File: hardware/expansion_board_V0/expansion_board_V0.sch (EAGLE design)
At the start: 109 parts, among them IC6 DRV8402, IC7 DRV8402, IC8 DRV8402, X10 M1-2, X11 M3-4, X14 M1-2, X15 M3-4, X18 M1-2, X19 M3-4

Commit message: Add some I/Os connectors
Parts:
- removed C48, C49, C50, C51: 100n, rcl:C-EUC0805
- removed C52, C53, C54, C55: 100n, rcl:C-EUC0603
- removed C56: 100n, rcl:C-EUC0603K
- removed IC8: DRV8402, etienne:DRV8402
- removed JP2, JP3, JP4: (no value), pinhead-2:PINHD-1X08_2.54
- removed X16, X17: (no value), con-phoenix-254:MPT2
- removed X18: M1-2, con-wago-500:W237-102
- removed X19: M3-4, con-wago-500:W237-102
- removed X2: (no value), con-phoenix-254:MPT4
- added C1, C2, C3, C6: 100n, rcl:C-EUC0805
- added C11, C7, C8, C9: 100n, rcl:C-EUC0603
- added C17: 100n, rcl:C-EUC0603K
- added IC1: DRV8402, etienne:DRV8402
- added J1, J10, J11, J12, J13, J14, J15, J16, J2, J24, J25, J26, J3, J4, J5, J6, J7, J8, J9: (no value), SparkFun-Connectors:M03LONGPADS
- added J17, J20, J21, J22: (no value), SparkFun-Connectors:M08LONGPADS
- added J18, J19: (no value), SparkFun-Connectors:M04JST
- added J23: (no value), SparkFun-Connectors:M04POLAR
- added J27, J28, J29, J30, J31, J32: (no value), SparkFun-Connectors:M03JST-PTH-VERT
- added R10, R12, R22, R23, R24, R25, R26, R27, R28, R29, R30, R31, R32, R33, R34, R35, R36, R37, R38, R39, R40, R41, R42, R43, R44, R45, R46, R47, R48, R49, R50, R9: (no value), resistor:R-EU_R0603
- added R51, R52: 33R, resistor:R-EU_R0603
- added X1, X3: (no value), con-phoenix-254:MPT2
- added X4: M1-2, con-wago-500:W237-102
- added X5: M3-4, con-wago-500:W237-102
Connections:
- removed net N$100: IC8.M2, R18.1
- removed net N$101: IC8.M3, R17.1
- removed net N$102: C50.2, IC8.BST_A
- removed net N$103: C49.2, IC8.BST_B
- removed net N$104: C48.1, IC8.BST_C
- removed net N$105: C51.1, IC8.BST_D
- removed net N$106: C56.2, IC8.AGND, R17.2, R18.2, R19.2, R20.2, R21.1
- removed net N$114: C56.1, IC8.VREG
- removed net N$115: IC8.OC_ADJ, R21.2
- removed net N$116: IC8.OTW, JP4.8
- removed net N$117: IC8.FAULT, JP4.7
- removed net N$118: IC8.PWM_A, JP4.6
- removed net N$119: IC8.RESET_AB, JP4.5
- removed net N$120: IC8.PWM_B, JP4.4
- removed net N$121: IC8.PWM_C, JP4.3
- removed net N$122: IC8.RESET_CD, JP4.2
- removed net N$123: IC8.PWM_D, JP4.1
- removed net N$5: X2-2.1
- removed net N$99: IC8.M1, R19.1
- new net /SS1: J18.1
- new net /SS2: J19.1
- new net AN_1: R35.2, R36.2
- new net AN_2: R37.2, R38.2
- new net AN_3: R39.2, R40.2
- new net AN_4: R41.2, R42.2
- new net AN_5: R43.2, R44.2
- new net AN_6: R45.2, R46.2
- new net AN_7: R47.2, R48.2
- new net AN_8: R49.2, R50.2
- new net D1: J20.8
- new net D2: J20.7
- new net D3: J20.6
- new net D4: J20.5
- new net D5: J20.4
- new net D6: J20.3
- new net D7: J20.2
- new net D8: J20.1
- new net IND_1: J27.1
- new net IND_2: J28.1
- new net IND_3: J29.1
- new net IND_4: J30.1
- new net IND_5: J31.1
- new net IND_6: J32.1
- new net MISO1: J18.4
- new net MISO2: J19.4
- new net MOSI1: J18.3, R51.1, R51.2
- new net MOSI2: J19.3, R52.1, R52.2
- new net N$10: J12.3, R41.1
- new net N$11: J2.3, R12.1
- new net N$12: J13.3, R43.1
- new net N$13: J3.3, R23.1
- new net N$14: J14.3, R45.1
- new net N$15: J4.3, R25.1
- new net N$16: J15.3, R47.1
- new net N$17: J5.3, R27.1
- new net N$18: J16.3, R49.1
- new net N$19: J6.3, R29.1
- new net N$2: J9.3, R35.1
- new net N$20: IC1.M1, R19.1
- new net N$22: IC1.M2, R18.1
- new net N$25: IC1.M3, R17.1
- new net N$26: C3.2, IC1.BST_A
- new net N$27: C2.2, IC1.BST_B
- new net N$28: C1.1, IC1.BST_C
- new net N$29: J7.3, R31.1
- new net N$30: C6.1, IC1.BST_D
- new net N$31: J8.3, R33.1
- new net N$32: C17.2, IC1.AGND, R17.2, R18.2, R19.2, R20.2, R21.1
- new net N$33: C17.1, IC1.VREG
- new net N$36: IC1.OC_ADJ, R21.2
- new net N$37: IC1.OTW, J22.8
- new net N$41: IC1.FAULT, J22.7
- new net N$47: IC1.PWM_A, J22.6
- new net N$50: IC1.RESET_AB, J22.5
- new net N$51: IC1.PWM_B, J22.4
- new net N$52: IC1.PWM_C, J22.3
- new net N$53: IC1.RESET_CD, J22.2
- new net N$54: IC1.PWM_D, J22.1
- new net N$7: J10.3, R37.1
- new net N$8: J11.3, R39.1
- new net N$9: J1.3, R9.1
- new net QEIA_1: J27.3
- new net QEIA_2: J28.3
- new net QEIA_3: J29.3
- new net QEIA_4: J30.3
- new net QEIA_5: J31.3
- new net QEIA_6: J32.3
- new net QEIB_1: J27.2
- new net QEIB_2: J28.2
- new net QEIB_3: J29.2
- new net QEIB_4: J30.2
- new net QEIB_5: J31.2
- new net QEIB_6: J32.2
- new net RX1: J24.3
- new net RX2: J25.3, J26.3
- new net SCLK1: J18.2
- new net SCLK2: J19.2
- new net SERV_1: R10.2, R9.2
- new net SERV_2: R12.2, R22.2
- new net SERV_3: R23.2, R24.2
- new net SERV_4: R25.2, R26.2
- new net SERV_5: R27.2, R28.2
- new net SERV_6: R29.2, R30.2
- new net SERV_7: R31.2, R32.2
- new net SERV_8: R33.2, R34.2
- new net TX1: J24.2
- new net TX2: J25.2, J26.2
- net +5V: now also J1.2, J10.2, J11.2, J12.2, J13.2, J14.2, J15.2, J16.2, J2.2, J3.2, J4.2, J5.2, J6.2, J7.2, J8.2, J9.2
- net FAULT2: now also IC7.FAULT, J21.7; no longer JP3.7
- net GND: now also C11.1, C7.1, C8.1, C9.1, IC1.GND, IC1.GND_A, IC1.GND_B, IC1.GND_C, IC1.GND_D, J1.1, J10.1, J11.1, J12.1, J13.1, J14.1, J15.1, J16.1, J2.1, J23.4, J24.1, J25.1, J26.1, J3.1, J4.1, J5.1, J6.1, J7.1, J8.1, J9.1, R10.1, R22.1, R24.1, R26.1, R28.1, R30.1, R32.1, R34.1, R36.1, R38.1, R40.1, R42.1, R44.1, R46.1, R48.1, R50.1; no longer C52.1, C53.1, C54.1, C55.1, IC8.GND, IC8.GND_A, IC8.GND_B, IC8.GND_C, IC8.GND_D, X2-4.1
- net GVDD: now also IC1.GVDD_A, IC1.GVDD_B, IC1.GVDD_C, IC1.GVDD_D, IC1.VDD, J23.1; no longer IC8.GVDD_A, IC8.GVDD_B, IC8.GVDD_C, IC8.GVDD_D, IC8.VDD, X2-1.1
- net M1A: now also C3.1, IC1.OUT_A, X1-1.1, X4-1.KL; no longer C50.1, IC8.OUT_A, X16-1.1, X18-1.KL
- net M1B: now also C2.1, IC1.OUT_B, X1-2.1, X4-2.KL; no longer C49.1, IC8.OUT_B, X16-2.1, X18-2.KL
- net M1C: now also C1.2, IC1.OUT_C, X3-1.1, X5-1.KL; no longer C48.2, IC8.OUT_C, X17-1.1, X19-1.KL
- net M1D: now also C6.2, IC1.OUT_D, X3-2.1, X5-2.KL; no longer C51.2, IC8.OUT_D, X17-2.1, X19-2.KL
- net N$38: now also J17.8; no longer JP2.8
- net N$39: now also J17.7; no longer JP2.7
- net N$40: now also J17.6; no longer JP2.6
- net N$42: now also J17.5; no longer JP2.5
- net N$43: now also J17.4; no longer JP2.4
- net N$44: now also J17.3; no longer JP2.3
- net N$45: now also J17.2; no longer JP2.2
- net N$46: now also J17.1; no longer JP2.1
- net N$6: now also J23.3; no longer X2-3.1
- net OTW2: now also IC7.OTW, J21.8; no longer JP3.8
- net PVDD: now also C11.2, C7.2, C8.2, C9.2, IC1.PVDD_A, IC1.PVDD_B, IC1.PVDD_C, IC1.PVDD_D; no longer C52.2, C53.2, C54.2, C55.2, IC8.PVDD_A, IC8.PVDD_B, IC8.PVDD_C, IC8.PVDD_D
- net PWM1_B: now also IC7.PWM_B, J21.4; no longer JP3.4
- net PWM1_C: now also IC7.PWM_C, J21.3; no longer JP3.3
- net PWM1_D: now also IC7.PWM_D, J21.1; no longer JP3.1
- net PWM2_A: now also IC7.PWM_A, J21.6; no longer JP3.6
- net RESET1_CD: now also IC7.RESET_CD, J21.2; no longer JP3.2
- net RESET2_AB: now also IC7.RESET_AB, J21.5; no longer JP3.5
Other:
- note added: "ADC"
- note added: "DIGITAL I/Os"
- note added: "QEIs"
- note added: "SERVOs"
- note added: "SPIs"
- note added: "UARTs"

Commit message: add qei
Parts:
- added C20: 100n, iocene:C_603
- added C21, C22, C27: 22p, iocene:C_603
- added R174, R176, R177, R179, R180, R182: 1k, iocene:R_603
- added R175, R178, R181: 100, iocene:R_603
- added U8: AM26C32, iocene:AM26C32
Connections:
- new net 5V: C20.P$2, U8.EN+, U8.VCC
- new net N$135: C21.P$2, R174.P$2, U8.A+
- new net N$136: C22.P$1, R179.P$2, U8.C-
- new net N$137: C27.P$2, R180.P$2, U8.D+
- new net N$138: C21.P$1, R176.P$2, U8.A-
- new net N$139: C22.P$2, R177.P$2, U8.C+
- new net N$142: C27.P$1, R182.P$2, U8.D-
- new net QEI0A: U8.C
- new net QEI0A+: R177.P$1, R178.P$1
- new net QEI0A-: R178.P$2, R179.P$1
- new net QEI0B: U8.D
- new net QEI0B+: R180.P$1, R181.P$1
- new net QEI0B-: R181.P$2, R182.P$1
- new net QEI0X: U8.A
- new net QEI0X+: R174.P$1, R175.P$1
- new net QEI0X-: R175.P$2, R176.P$1
- net GND: now also C20.P$1, U8.B+, U8.B-, U8.EN-, U8.GND

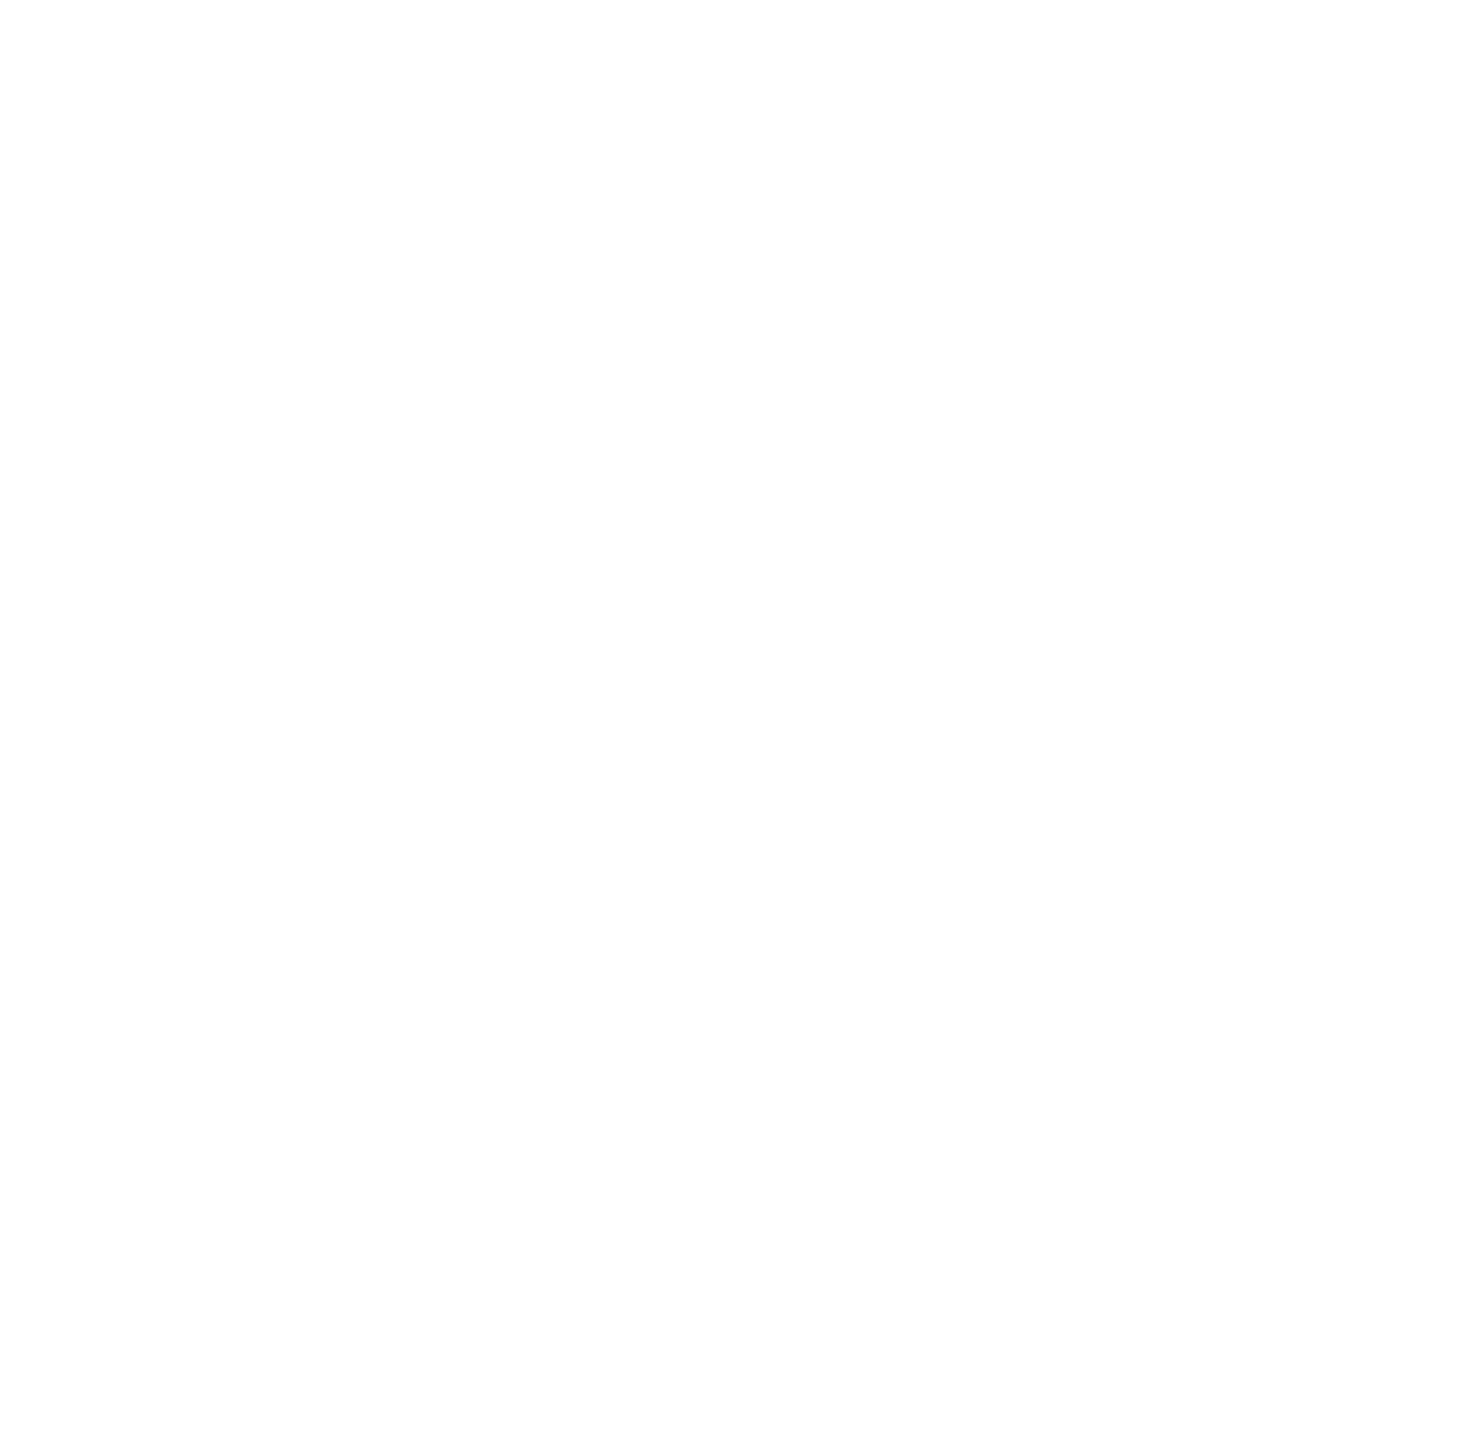
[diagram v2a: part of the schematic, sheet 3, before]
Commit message: hub usb
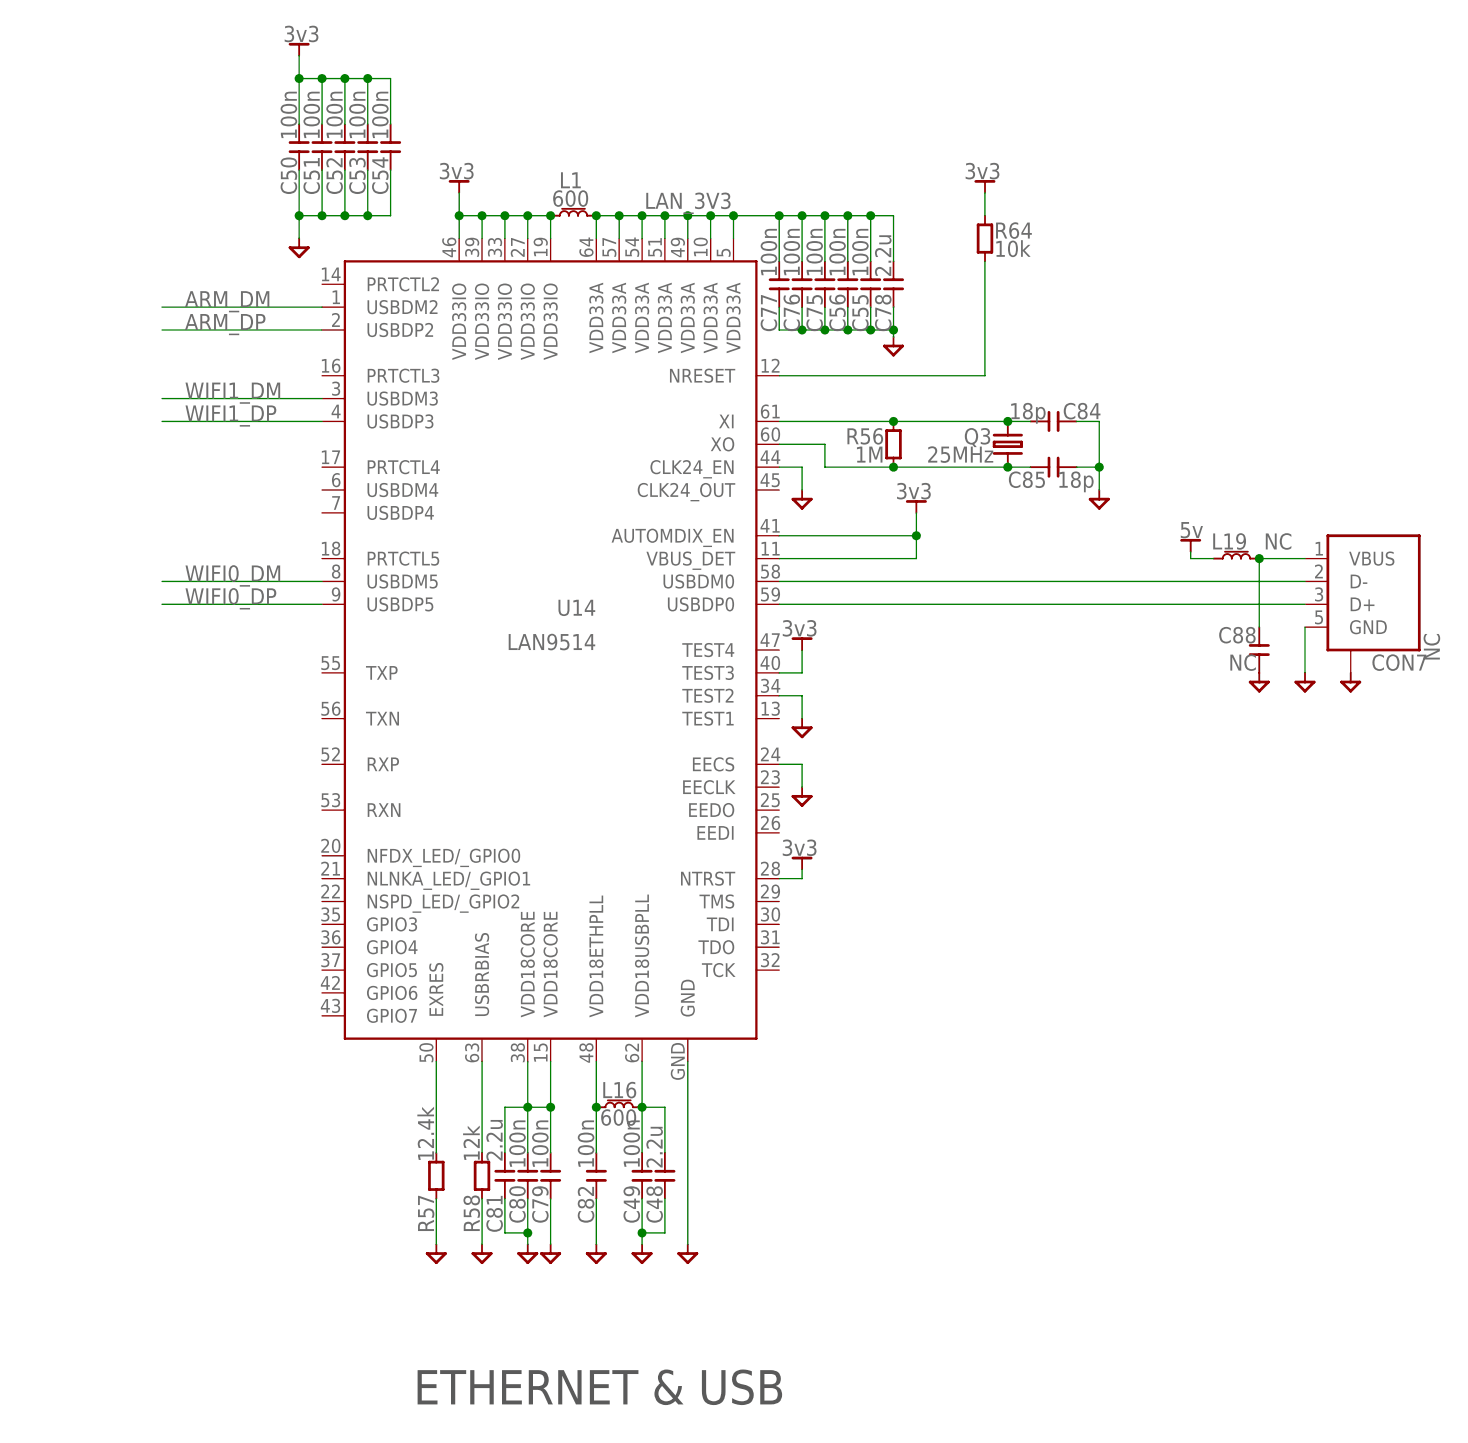
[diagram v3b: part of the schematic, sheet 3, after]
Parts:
- added C48, C78, C81: 2.2u, iocene:C_603
- added C49, C50, C51, C52, C53, C54, C55, C56, C75, C76, C77, C79, C80, C82: 100n, iocene:C_402
- added C84, C85: 18p, iocene:C_402
- added C88: NC, iocene:C_402
- added CON7: NC, iocene:USBUSB3140
- added L1, L16: 600, iocene:INDUCTANCE_603
- added L19: NC, iocene:INDUCTANCE_603
- added Q3: 25MHz, iocene:QUARTZ2
- added R56: 1M, iocene:R_402
- added R57: 12.4k, iocene:R_402
- added R58: 12k, iocene:R_402
- added R64: 10k, iocene:R_402
- added U14: LAN9514, iocene:LAN9514
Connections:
- new net 3V3: C50.P$2, C51.P$2, C52.P$2, C53.P$2, C54.P$2, L1.1, R64.P$2, U14.AUTOMDIX_EN, U14.NTRST, U14.TEST3, U14.VBUS_DET, U14.VDD33IO, U14.VDD33IO@1, U14.VDD33IO@2, U14.VDD33IO@3, U14.VDD33IO@4
- new net ARM_DM: U14.USBDM2
- new net ARM_DP: U14.USBDP2
- new net LAN_3V3: C55.P$2, C56.P$2, C75.P$2, C76.P$2, C77.P$2, C78.P$2, L1.2, U14.VDD33A, U14.VDD33A@1, U14.VDD33A@2, U14.VDD33A@3, U14.VDD33A@4, U14.VDD33A@5, U14.VDD33A@6
- new net N$55: C79.P$2, C80.P$2, C81.P$2, U14.VDD18CORE, U14.VDD18CORE@1
- new net N$56: R58.P$2, U14.USBRBIAS
- new net N$57: C48.P$2, C49.P$2, L16.2, U14.VDD18USBPLL
- new net N$600: R64.P$1, U14.NRESET
- new net N$62: R57.P$2, U14.EXRES
- new net N$65: C82.P$2, L16.1, U14.VDD18ETHPLL
- new net N$81: C85.P$2, Q3.2, R56.P$1, U14.XO
- new net N$82: CON7.D+, U14.USBDP0
- new net N$89: C88.P$2, CON7.VBUS, L19.2
- new net N$90: CON7.D-, U14.USBDM0
- new net N$91: C84.P$2, Q3.1, R56.P$2, U14.XI
- new net WIFI0_DM: U14.USBDM5
- new net WIFI0_DP: U14.USBDP5
- new net WIFI1_DM: U14.USBDM3
- new net WIFI1_DP: U14.USBDP3
- net 5V: now also L19.1
- net GND: now also C48.P$1, C49.P$1, C50.P$1, C51.P$1, C52.P$1, C53.P$1, C54.P$1, C55.P$1, C56.P$1, C75.P$1, C76.P$1, C77.P$1, C78.P$1, C79.P$1, C80.P$1, C81.P$1, C82.P$1, C84.P$1, C85.P$1, C88.P$1, CON7.GND, CON7.GND@2, R57.P$1, R58.P$1, U14.CLK24_EN, U14.EECS, U14.GND, U14.TEST2
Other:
- note added: "ETHERNET & USB"
